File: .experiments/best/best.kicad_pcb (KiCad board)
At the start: 2 copper layers, 140 x 90 mm, 39 parts, among them J1 USB_C, J2 Output, J3 Debug, Q1 FS8205A, U1 USBLC6-2SC6, U2 BQ24072, U3 HY2113-KB5B, U4 MT3608, U5 AP2112K-3.3, U6 LN61CN3302MR-G

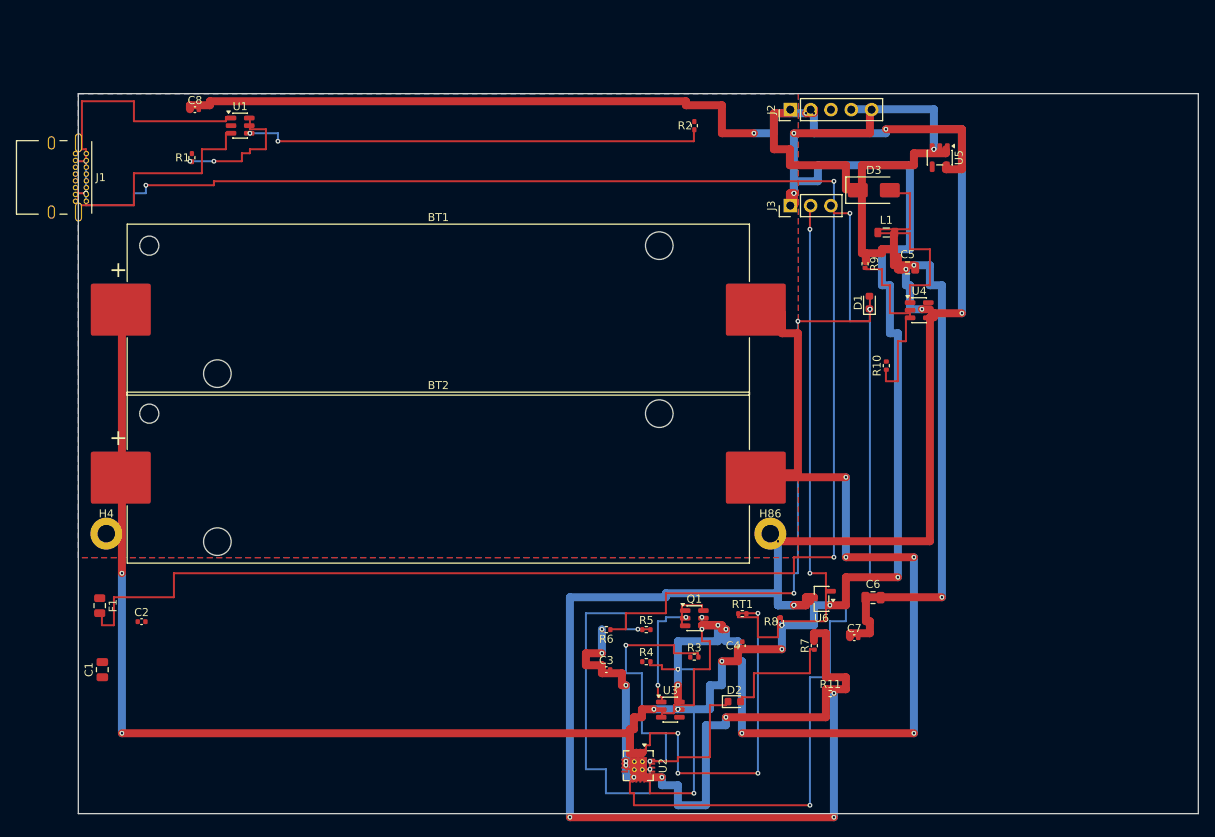
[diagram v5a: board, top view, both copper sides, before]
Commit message: 100-round experiment: best score 2.7, 26/26 nets routed, GIF collected
Co-Authored-By: Claude Sonnet 4.6 <noreply@anthropic.com>
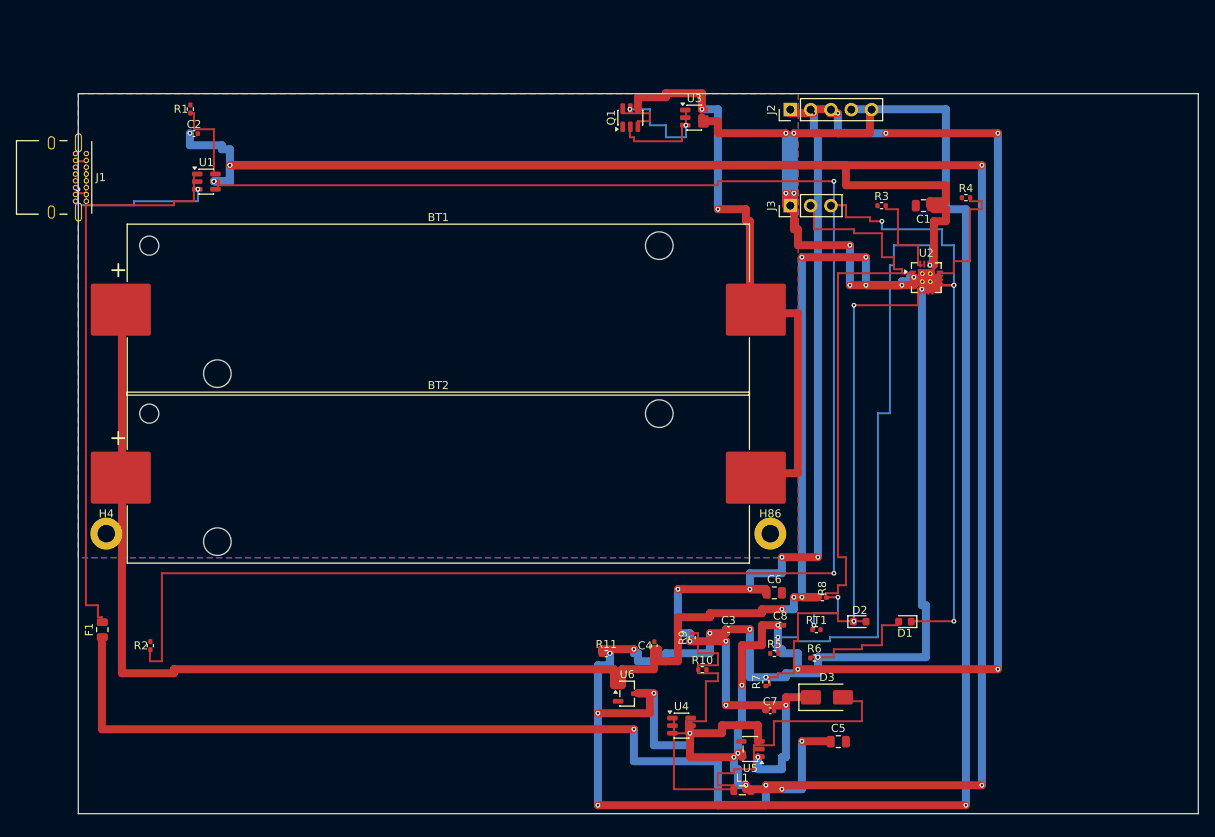
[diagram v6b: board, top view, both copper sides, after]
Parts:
- moved C1 117.9 mm to (105.6, 14.0), turned to 180 degrees
- moved C8 97.5 mm to (87.7, 66.4)
- moved R2 94.1 mm to (9.00, 69.0)
- moved U5 77.6 mm to (84.0, 81.9), turned to 180 degrees
- moved U3 74.1 mm to (77.0, 3.00)
- moved L1 72.0 mm to (83.0, 87.1)
- moved U2 70.8 mm to (106.0, 23.0), turned to 0 degrees
- moved R4 70.4 mm to (111.0, 13.0)
- moved D3 63.7 mm to (93.6, 75.5)
- moved Q1 63.1 mm to (69.0, 3.00), turned to 90 degrees
- moved C2 61.4 mm to (14.5, 5.00)
- moved R3 61.1 mm to (100.4, 14.0)
- moved C5 59.8 mm to (95.0, 81.0)
- moved U4 59.8 mm to (75.4, 79.0)
- moved R9 51.5 mm to (76.7, 68.0), turned to 90 degrees
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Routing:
- net /VBUS: track 0.00 -> 433.5 mm, vias 0 -> 10
- net Net-(F1-Pad2): track 253.0 -> 61.5 mm, vias 6 -> 0
- net Net-(R2-Pad1): track 58.0 -> 225.5 mm
- net /CELL_NEG: track 140.5 -> 75.5 mm, vias 8 -> 2
- net Net-(D1-A): track 74.0 -> 15.5 mm, vias 2 -> 0
- net /CHG_N: track 117.0 -> 77.0 mm
- net /3V3: track 115.5 -> 148.5 mm, vias 4 -> 8
- net /NTC_SENSE: track 115.0 -> 83.5 mm, vias 6 -> 2
- net Net-(U2-TMR): track 43.5 -> 73.5 mm
- net Net-(D2-K): track 21.5 -> 51.0 mm, vias 0 -> 2
- net /VSYS: track 83.0 -> 105.0 mm
- net Net-(D3-A): track 29.5 -> 50.5 mm
- net Net-(U2-ISET): track 32.0 -> 12.0 mm, vias 2 -> 0
- net /VSYS_BOOST: track 14.0 -> 31.5 mm, vias 2 -> 4
- net /5V: track 120.5 -> 135.0 mm, vias 2 -> 10
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
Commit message: 200-round experiment: router + scoring improvements
- 8-connected A* grid with octile heuristic and corner-cut prevention
- Trace cost weight 0.1->0.5, base cost 1000->100 for balanced detours
- Shorts penalty numerator 0.1->1.0 (less punishing, preserves gradient)

Co-Authored-By: Claude Sonnet 4.6 <noreply@anthropic.com>
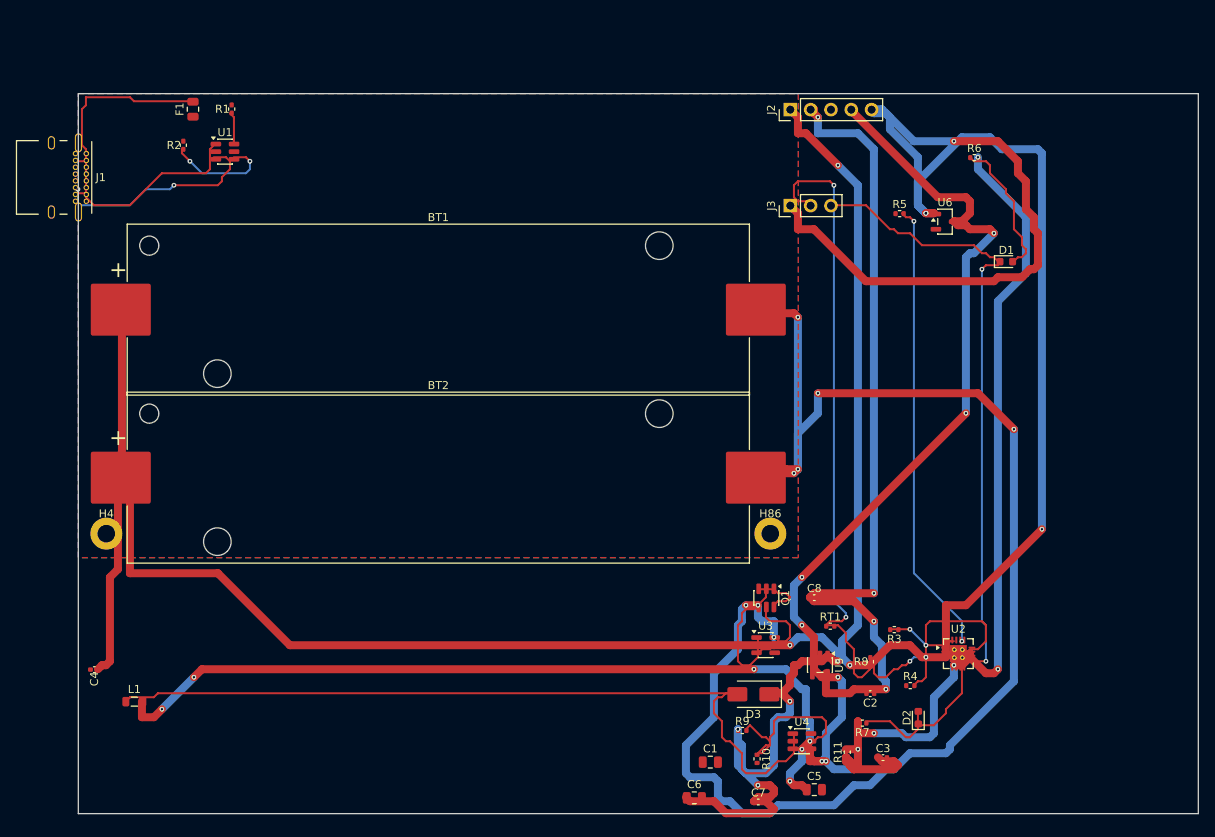
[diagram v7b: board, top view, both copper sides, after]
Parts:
- moved C2 109.8 mm to (99.0, 75.0), turned to 180 degrees
- moved L1 76.8 mm to (7.00, 76.0)
- moved C1 74.5 mm to (79.0, 83.6), turned to 0 degrees
- moved U6 71.1 mm to (108.3, 16.0)
- moved C4 70.1 mm to (2.00, 72.0), turned to 180 degrees
- moved U3 66.5 mm to (85.9, 68.9)
- moved F1 66.0 mm to (14.3, 1.94)
- moved R6 65.7 mm to (112.0, 8.00)
- moved R2 62.7 mm to (13.1, 6.45)
- moved Q1 62.4 mm to (86.0, 63.0), turned to -90 degrees
- moved R4 61.4 mm to (104.0, 74.0)
- moved R5 57.2 mm to (102.7, 15.0)
- moved R3 53.0 mm to (102.0, 67.0), turned to 180 degrees
- moved U2 47.2 mm to (110.0, 70.0)
- moved D1 46.8 mm to (116.0, 21.0), turned to 0 degrees
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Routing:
- net /VBUS: track 433.5 -> 0.00 mm, vias 10 -> 0
- net Net-(R2-Pad1): track 225.5 -> 13.4 mm
- net /CELL_NEG: track 75.5 -> 187.8 mm, vias 2 -> 8
- net /EN: track 213.5 -> 125.0 mm
- net /VSYS_BOOST: track 31.5 -> 104.0 mm, vias 4 -> 6
- net /VBAT: track 282.5 -> 351.6 mm, vias 14 -> 8
- net Net-(D3-A): track 50.5 -> 100.8 mm
- net /3V3: track 148.5 -> 103.8 mm, vias 8 -> 4
- net Net-(D2-K): track 51.0 -> 10.9 mm, vias 2 -> 0
- net Net-(F1-Pad2): track 61.5 -> 28.1 mm
- net Net-(U2-TMR): track 73.5 -> 56.9 mm
- net Net-(D2-A): track 22.5 -> 9.74 mm
- net /VSYS: track 105.0 -> 115.5 mm, vias 8 -> 4
- net /NTC_SENSE: track 83.5 -> 92.8 mm, vias 2 -> 4
- net Net-(J1-CC2): track 19.0 -> 26.4 mm
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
